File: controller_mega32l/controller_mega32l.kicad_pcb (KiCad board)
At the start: 2 copper layers, 156 x 100 mm, 80 parts, among them IC1 ATMEGA32-A, IC2 MAX481CPA, J1 RJ45, K1 CONN_PWR_OUT, P1 CONN_PWR_IN, P2 CONN_PWM_OUT, P3 CONN_3X2, P4 CONN_JTAG, P5 CONN_ADC, P6 CONN_GPIO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

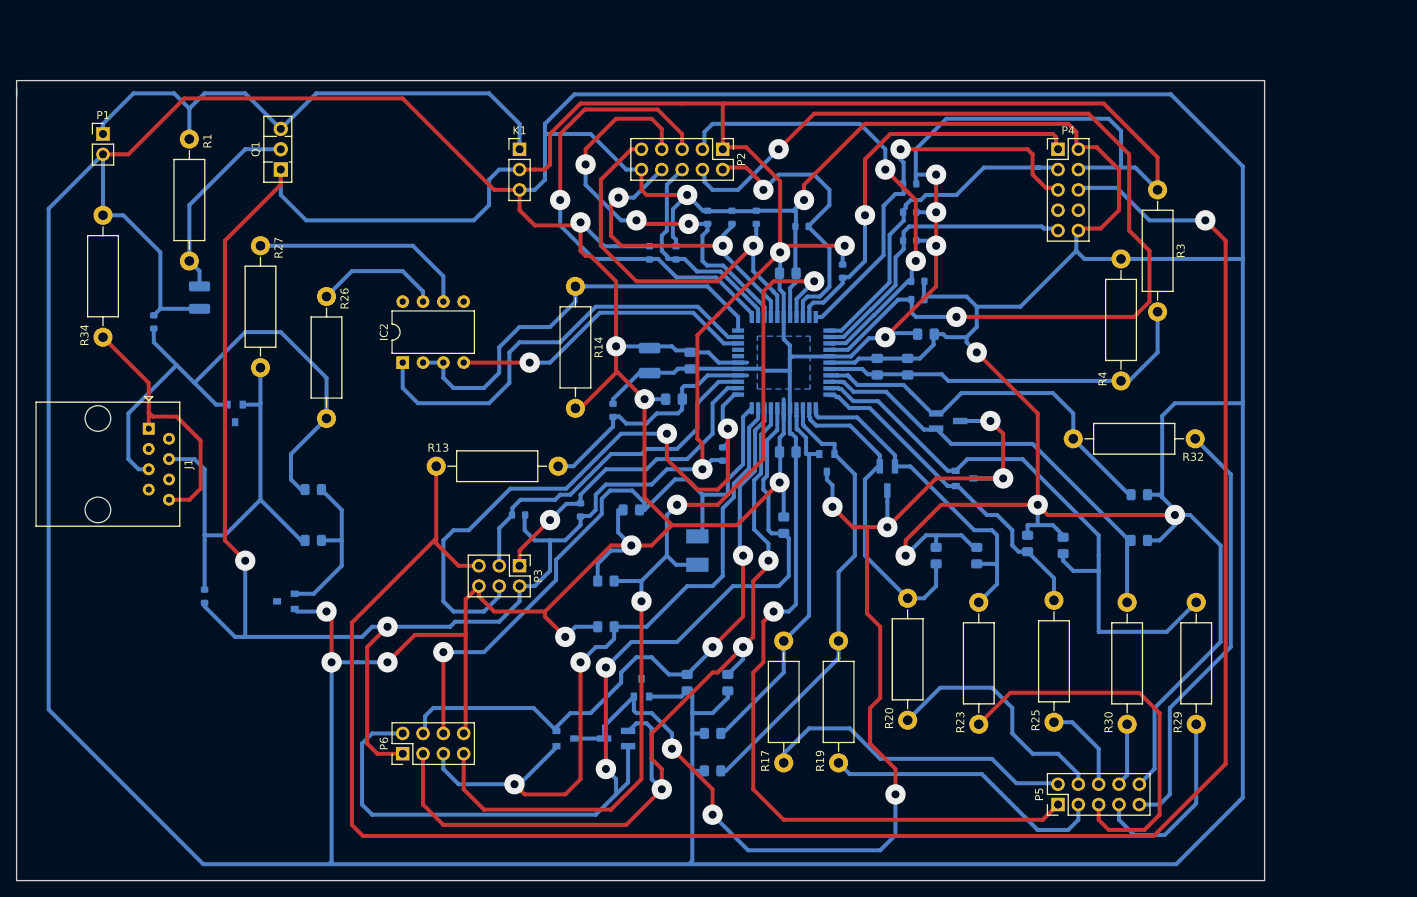
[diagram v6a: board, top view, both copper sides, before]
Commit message: power lines optimization
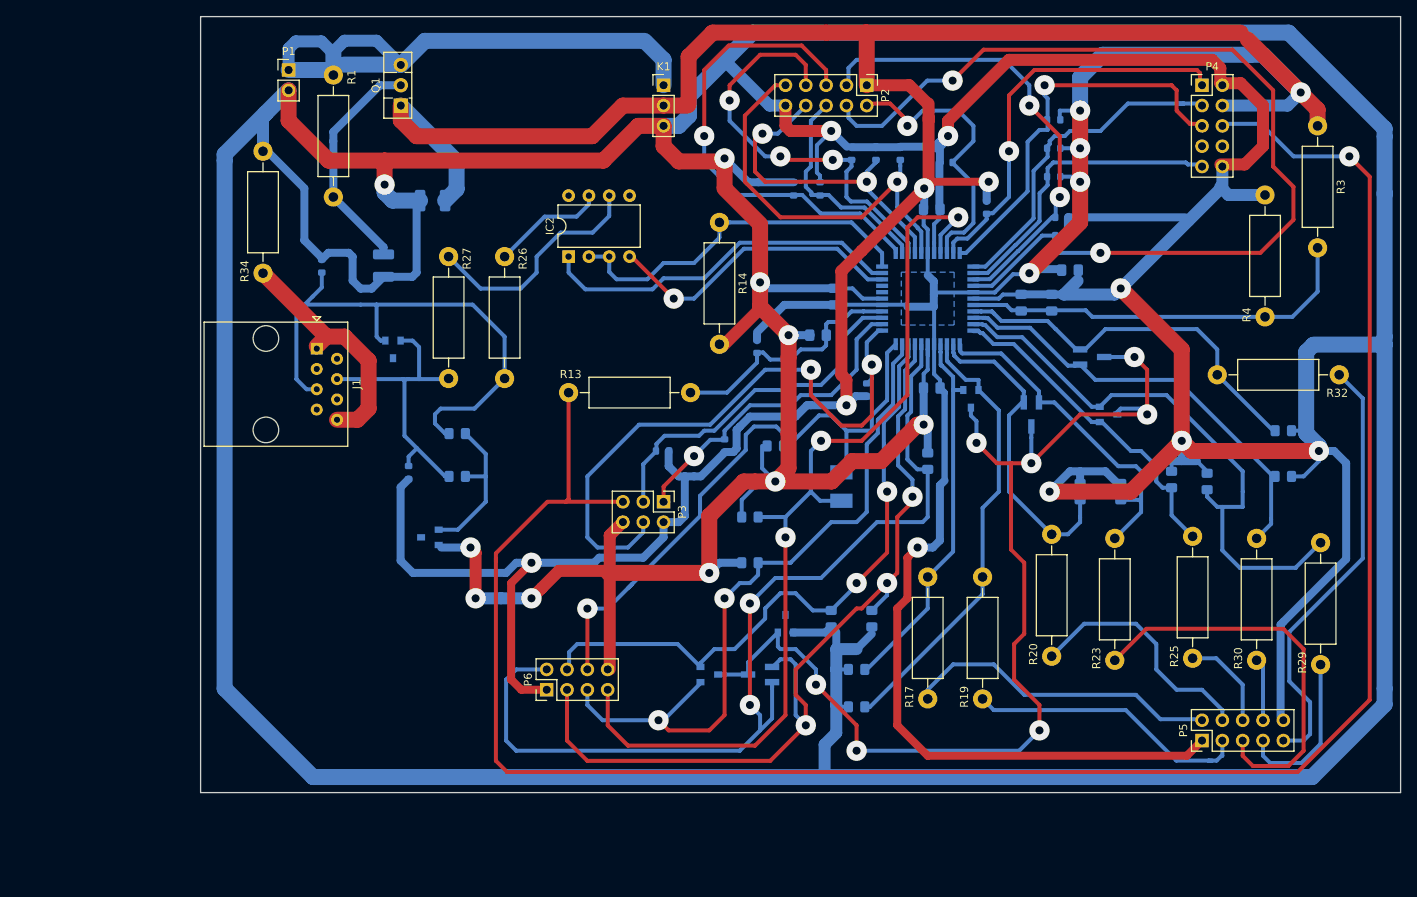
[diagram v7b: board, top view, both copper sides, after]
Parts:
- moved C1 33.7 mm to (92.0, 75.0), turned to 180 degrees
- moved R31 29.8 mm to (89.0, 109.0)
- moved IC2 24.6 mm to (109.0, 82.0)
- moved P1 24.5 mm to (74.0, 58.7)
- moved R27 23.6 mm to (94.0, 82.0)
- moved D1 23.3 mm to (85.9, 83.1)
- moved J1 23.3 mm to (77.5, 93.5)
- moved R26 22.8 mm to (101.0, 82.0)
- moved R33 22.1 mm to (78.2, 83.2)
- moved R3 21.5 mm to (202.6, 65.7)
- moved R34 21.5 mm to (70.8, 84.1)
- moved D15 21.3 mm to (87.0, 93.6)
- moved R10 19.7 mm to (144.4, 69.1)
- moved R16 19.7 mm to (128.5, 105.7)
- moved D19 19.7 mm to (136.1, 127.9)
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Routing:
- net +5VD: track 600.1 -> 560.0 mm
- net DGND: track 1137.0 -> 1105.4 mm, vias 15 -> 16
- net Net-(D15-Pad2): track 55.3 -> 38.1 mm
- net +24V: track 68.7 -> 77.8 mm
- net Net-(IC1-Pad10): track 54.7 -> 46.0 mm
- net Net-(IC1-Pad11): track 53.3 -> 46.3 mm
- net Net-(D14-Pad3): track 146.6 -> 140.7 mm
- net Net-(D1-Pad2): track 25.0 -> 28.8 mm
- net Net-(P5-Pad7): track 23.9 -> 20.4 mm
- net Net-(C2-Pad1): track 48.2 -> 51.5 mm
- net /-RESET: track 256.7 -> 258.9 mm
- net Net-(J1-Pad1): track 32.3 -> 30.3 mm
- net Net-(IC2-Pad6): track 27.6 -> 29.2 mm
- net Net-(D10-Pad2): track 74.4 -> 73.0 mm
- net Net-(IC2-Pad7): track 15.7 -> 14.3 mm
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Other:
- board size 156 x 100 mm -> 150 x 97 mm

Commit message: Output RJ-45 Interfaces added
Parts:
- added J_Out1: 8P8C_Shielded, Connector_RJ:RJ45_Amphenol_54602-x08_Horizontal, F.Cu at (78.0, 109.0)
- added J_Out2: 8P8C_Shielded, Connector_RJ:RJ45_Amphenol_54602-x08_Horizontal, F.Cu at (78.0, 127.0)
- moved IC2 8.00 mm to (109.0, 90.0)
- moved D15 4.70 mm to (88.0, 89.0), turned to 270 degrees
- moved J1 3.00 mm to (77.5, 90.5)
- moved R34 2.08 mm to (70.8, 82.0)
- moved D1 2.00 mm to (85.9, 81.1)
- moved R33 2.00 mm to (78.2, 81.2)
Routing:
- net Net-(J1-Pad1): track 30.3 -> 90.6 mm
- net Net-(D15-Pad2): track 38.1 -> 78.3 mm
- net Net-(D13-Pad2): track 68.9 -> 101.8 mm
- net +5VD: track 560.0 -> 577.0 mm
- net Net-(IC1-Pad10): track 46.0 -> 53.0 mm
- net Net-(IC2-Pad6): track 29.2 -> 25.6 mm
- net DGND: track 1105.4 -> 1109.0 mm
- net Net-(IC1-Pad11): track 46.3 -> 44.7 mm
- net /GPIO_5: track 77.7 -> 78.7 mm
- net Net-(IC1-Pad9): track 37.9 -> 37.0 mm
- net Net-(D1-Pad2): track 28.8 -> 27.9 mm
- net Net-(IC2-Pad7): track 14.3 -> 13.5 mm
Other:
- outline, holes or cut-outs redrawn
- board text added: "3 * RS-485"
